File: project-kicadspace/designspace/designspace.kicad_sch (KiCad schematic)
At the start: 0 parts

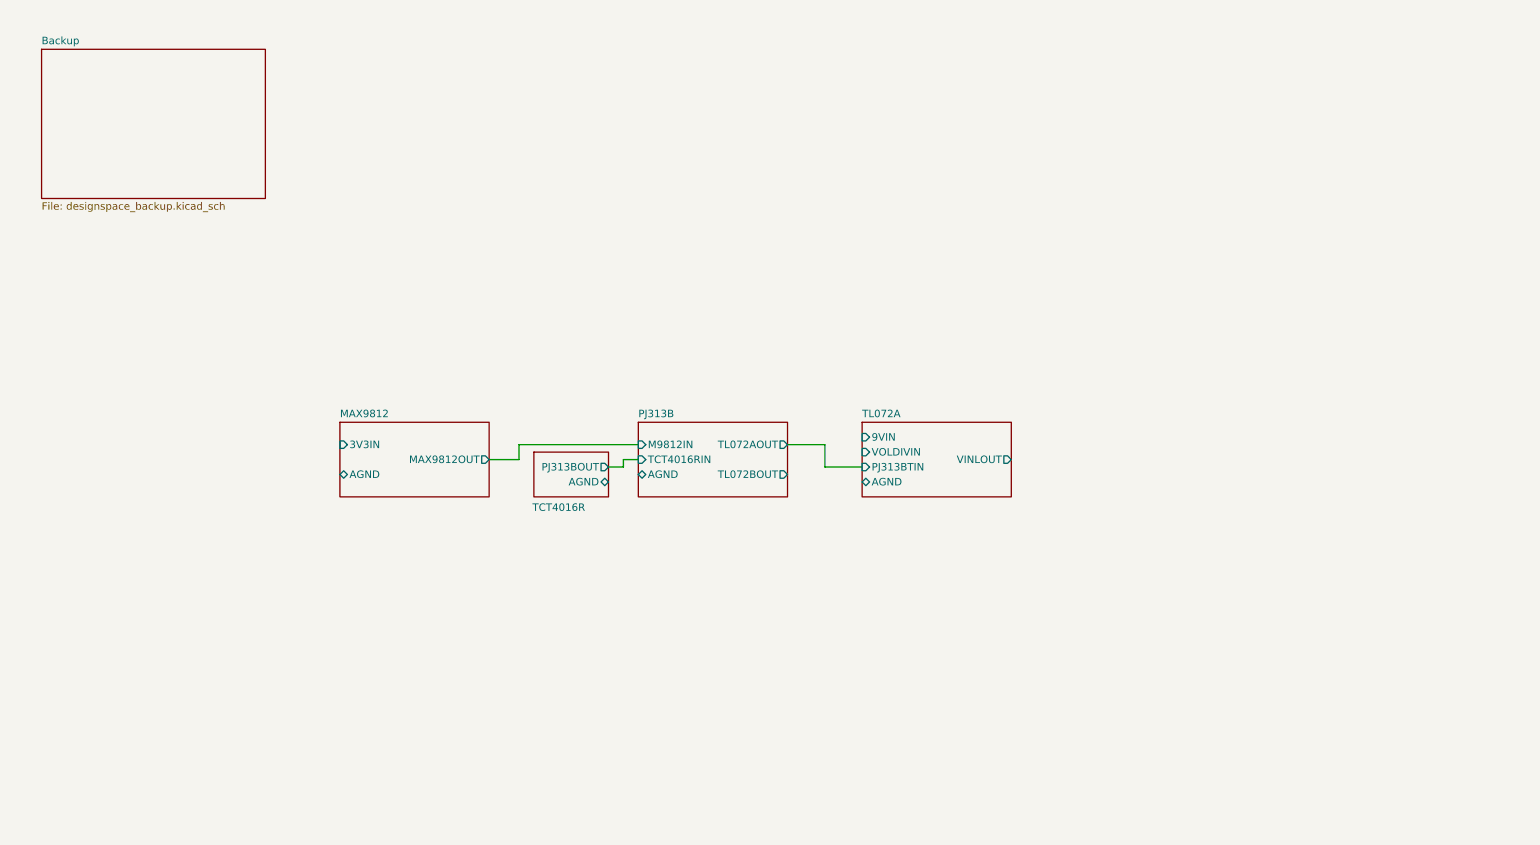
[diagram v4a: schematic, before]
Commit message: feat(sch): remove hierachical structure and add import footprint
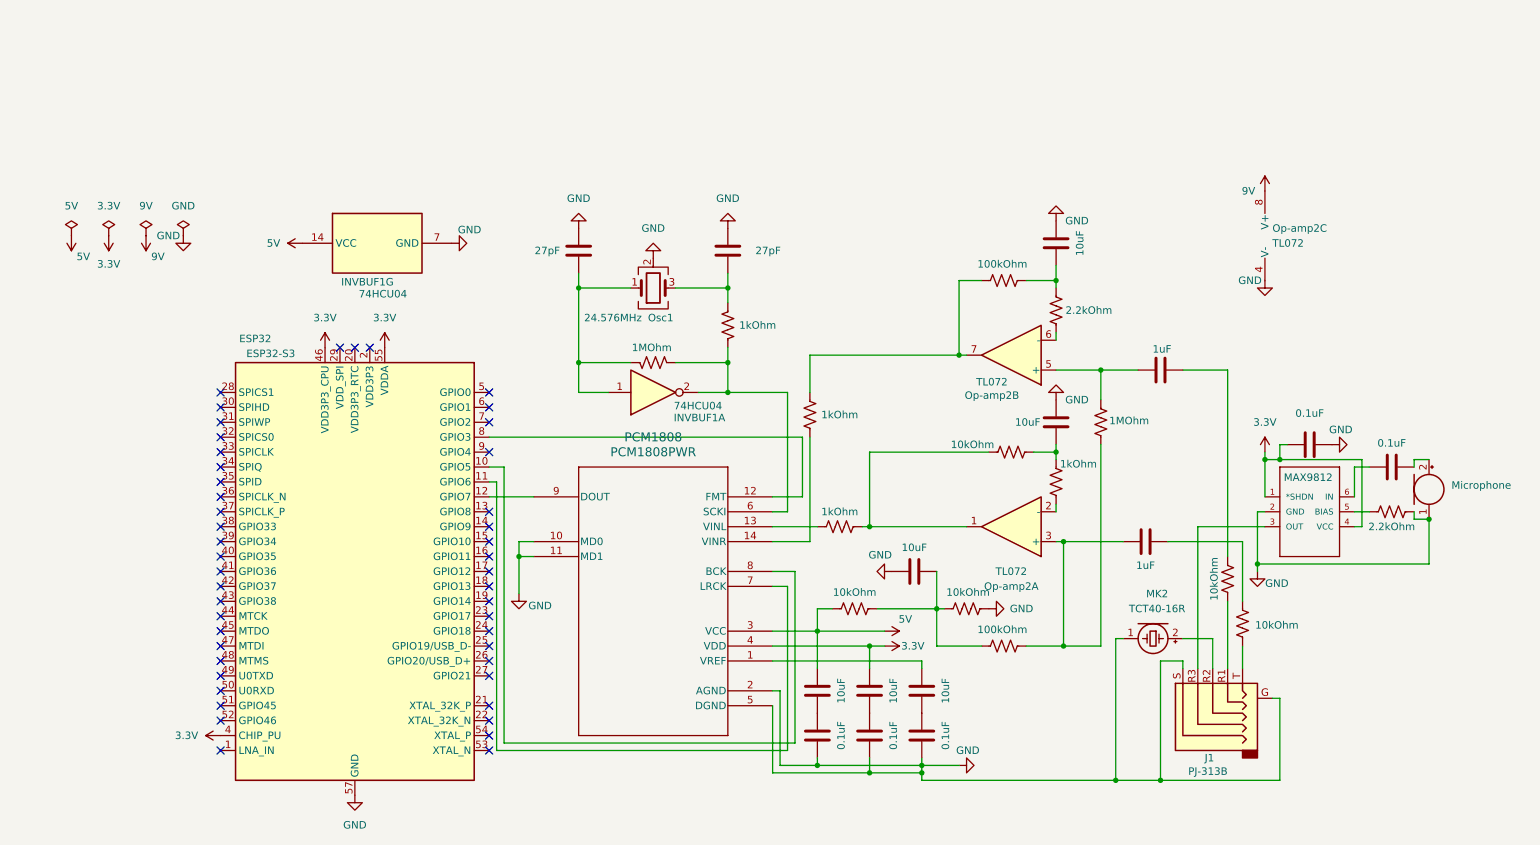
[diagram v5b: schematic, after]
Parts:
- added C1, C2, C5, C7, C9: 0.1uF, Capacitor_SMD:C_0805_2012Metric, symbol Device:C
- added C10, C13, C14, C4, C6, C8: 10uF, Capacitor_SMD:C_0805_2012Metric, symbol Device:C
- added C11, C12: 27pF, Capacitor_SMD:C_0805_2012Metric, symbol Device:C
- added C15, C3: 1uF, Capacitor_SMD:C_0805_2012Metric, symbol Device:C
- added ESP32: ESP32-S3, RF_Module:ESP32-S3-WROOM-1, symbol MCU_Espressif:ESP32-S3
- added INVBUF1: 74HCU04, Package_SO:SO-14_5.3x10.2mm_P1.27mm, symbol 74xx:74HC04
- added J1: PJ-313B, Connector_Audio:Jack_3.5mm_PJ311_Horizontal, symbol Connector_Audio:AudioJack5_Ground
- added MK1: Microphone, Sensor_Audio:POM-2244P-C3310-2-R, symbol Device:Microphone
- added MK2: TCT40-16R, tct4016r:TCT40-16R, symbol Device:Microphone_Ultrasound
- added Op-amp2: TL072, tl072:TL072IDT, symbol Amplifier_Operational:TL072
- added Osc1: 24.576MHz, Crystal:Crystal_SMD_7050-4Pin_7.0x5.0mm, symbol Device:Crystal_GND24
- added PCM1808: PCM1808PWR, pw14:PW14, symbol PCM1808:PCM1808PWR
- added R1, R14: 2.2kOhm, Resistor_SMD:R_0805_2012Metric, symbol Device:R_US
- added R10, R11, R2, R3, R4: 10kOhm, Resistor_SMD:R_0805_2012Metric, symbol Device:R_US
- added R12, R8: 1MOhm, Resistor_SMD:R_0805_2012Metric, symbol Device:R_US
- added R13, R7: 100kOhm, Resistor_SMD:R_0805_2012Metric, symbol Device:R_US
- added R15, R5, R6, R9: 1kOhm, Resistor_SMD:R_0805_2012Metric, symbol Device:R_US
- added U3: MAX9812, tl072:TL072IDT, symbol MAX9812:MAX9812
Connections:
- new net: J1.R3, U3.3 (OUT)
- new net: R1.1, U3.5 (BIAS)
- new net: C1.1, U3.6 (IN)
- new net: C4.2, C5.2
- new net: C15.1, Op-amp2.5 (+), R12.1
- new net: C15.2, R11.1
- new net: C13.2, R2.2, R3.1, R7.1
- new net: ESP32.10 (GPIO5), PCM1808.8 (BCK)
- new net: ESP32.11 (GPIO6), PCM1808.7 (LRCK)
- new net: ESP32.12 (GPIO7), PCM1808.9 (DOUT)
- new net: ESP32.2 (VDD3P3), ESP32.3 (VDD3P3)
- new net: ESP32.8 (GPIO3), PCM1808.12 (FMT)
- new net: C14.2, R13.2, R14.2
- new net: Op-amp2.6 (-), R14.1
- new net: Op-amp2.7, R13.1, R15.2
- new net: C3.1, Op-amp2.3 (+), R12.2, R7.2
- new net: J1.R2, MK2.2 (+)
- new net: C3.2, R10.1
- new net: J1.T, R10.2
- new net: Op-amp2.2 (-), R5.1
- new net: C10.2, R4.2, R5.2
- new net: Op-amp2.1, R4.1, R6.1
- new net: C6.1, PCM1808.1 (VREF)
- new net: PCM1808.13 (VINL), R6.2
- new net: PCM1808.14 (VINR), R15.1
- new net: INVBUF1.2, PCM1808.6 (SCKI), R8.2, R9.2
- new net: C6.2, C7.2
- new net: C8.2, C9.2
- new net: C11.1, INVBUF1.1, Osc1.1, R8.1
- new net: C12.1, Osc1.3, R9.1
- new net: J1.R1, R11.2
- new net: C1.2, MK1.2 (+)
- new net 3.3V: C2.1, C8.1, ESP32.4 (CHIP_PU), ESP32.46 (VDD3P3_CPU), ESP32.55 (VDDA), ESP32.56 (VDDA), PCM1808.4 (VDD), U3.1 (*SHDN), U3.4 (VCC)
- new net 5V: C4.1, INVBUF1.14 (VCC), PCM1808.3 (VCC), R2.1
- new net 9V: Op-amp2.8 (V+)
- new net GND: C10.1, C11.2, C12.2, C13.1, C14.1, C2.2, C5.1, C7.1, C9.1, ESP32.57 (GND), INVBUF1.7 (GND), J1.G, J1.S, MK1.1 (-), MK2.1 (-), Op-amp2.4 (V-), Osc1.2 (G), Osc1.4 (G), PCM1808.10 (MD0), PCM1808.11 (MD1), PCM1808.2 (AGND), PCM1808.5 (DGND), R1.2, R3.2, U3.2 (GND)
- no-connect marks 0 -> 47
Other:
- removed sheet Backup
- removed sheet MAX9812
- removed sheet PJ313B
- removed sheet TCT4016R
- removed sheet TL072A

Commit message: feat(pcb): resolve footprint errors and implement routing between pcm1808, max9812, tct4016r, pj342s
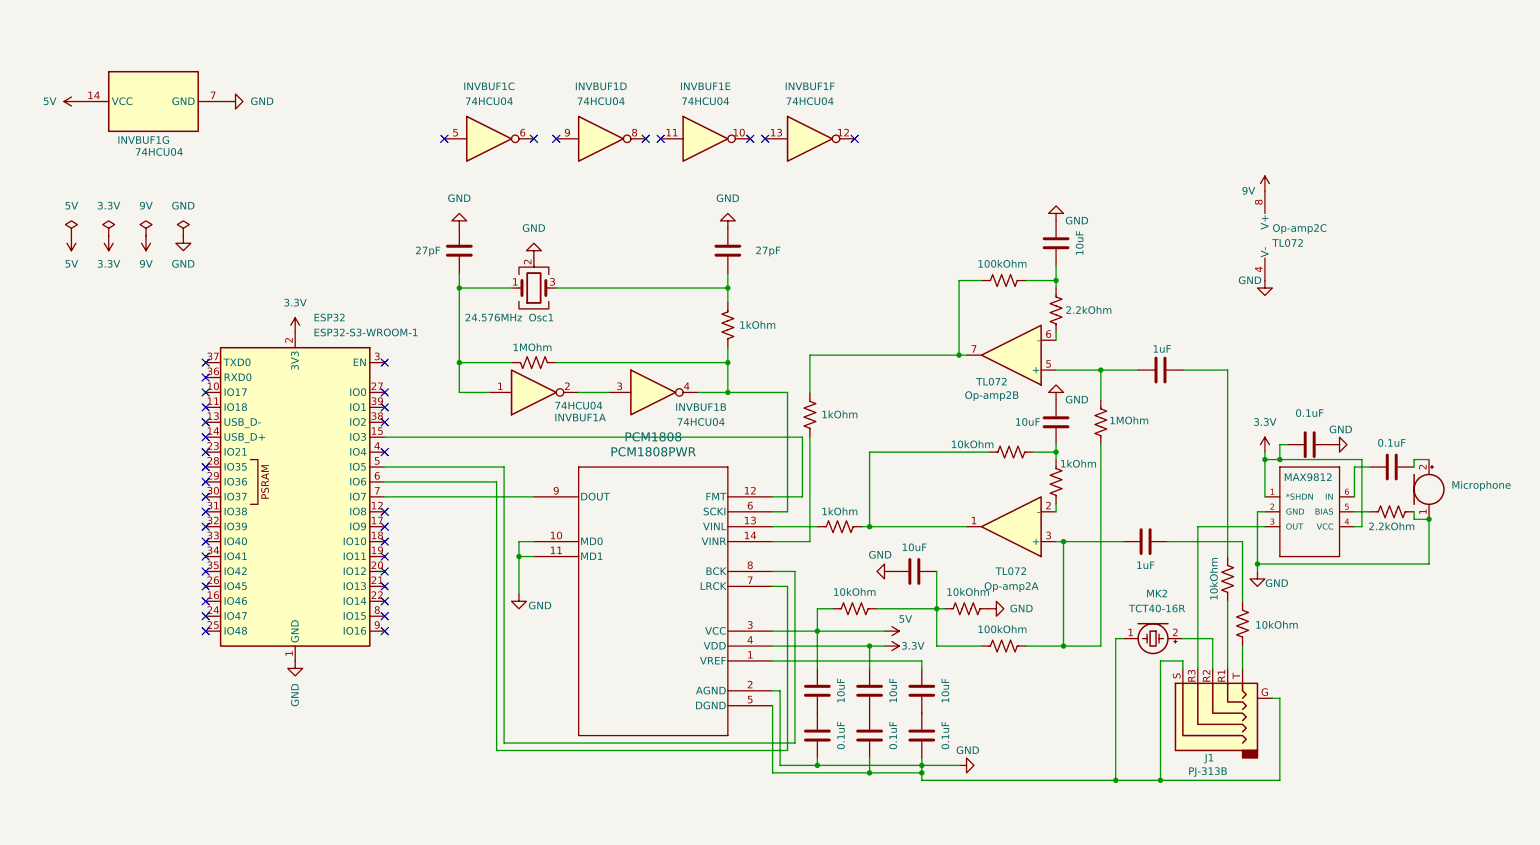
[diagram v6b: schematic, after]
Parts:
- removed ESP32: ESP32-S3, RF_Module:ESP32-S3-WROOM-1, symbol MCU_Espressif:ESP32-S3
- added ESP32: ESP32-S3-WROOM-1, RF_Module:ESP32-S3-WROOM-1, symbol RF_Module:ESP32-S3-WROOM-1
- added unit 3 of INVBUF1
- added unit 6 of INVBUF1
- added unit 5 of INVBUF1
- added unit 2 of INVBUF1
- added unit 4 of INVBUF1
- J1: footprint Connector_Audio:Jack_3.5mm_PJ311_Horizontal -> pj342s:pj342s audio jack
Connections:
- net 3.3V: now also ESP32.2 (3V3)
- net GND: now also ESP32.1 (GND), ESP32.40 (GND), ESP32.41 (GND)
- net at PCM1808.8 (BCK): now also ESP32.5 (IO5)
- net at PCM1808.7 (LRCK): now also ESP32.6 (IO6)
- net at PCM1808.9 (DOUT): now also ESP32.7 (IO7)
- net at PCM1808.12 (FMT): now also ESP32.15 (IO3)
- net at PCM1808.6 (SCKI), R8.2, R9.2: now also INVBUF1.4; no longer INVBUF1.2
- new net: INVBUF1.2, INVBUF1.3
- no-connect marks 47 -> 41
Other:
- moved on the sheet: INVBUF1A, INVBUF1G, Osc1

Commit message: feat(pcb): add kit footprint for esp32 & inital placing
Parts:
- removed ESP32: ESP32-S3-WROOM-1, RF_Module:ESP32-S3-WROOM-1, symbol RF_Module:ESP32-S3-WROOM-1
- added ESP32: ESP32-S3-DEVKITC-1-N8R8, esp32-s3-kit:ESP32-S3-DEVKITC-1-N8R8, symbol ESP32-S3-DEVKITC-1-N8R8:ESP32-S3-DEVKITC-1-N8R8
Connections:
- net 3.3V: now also ESP32.3V3, ESP32.3V3.
- net GND: now also C6.2, ESP32.GND, ESP32.GND1, ESP32.GND2, ESP32.GND3; no longer C7.1, PCM1808.10 (MD0), PCM1808.11 (MD1)
- net at C13.2, R2.2, R3.1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: now also R12.2
- net at C3.1, Op-amp2.3 (+), R7.2: no longer R12.2
- net at PCM1808.1 (VREF): now also C7.2; no longer C6.1
- net at PCM1808.12 (FMT): now also ESP32.GPIO15
- net at PCM1808.7 (LRCK): now also ESP32.GPIO6
- net at PCM1808.8 (BCK): now also ESP32.GPIO5
- net at PCM1808.9 (DOUT): now also ESP32.GPIO7
- new net: ESP32.GPIO16, PCM1808.10 (MD0)
- new net: ESP32.GPIO17, PCM1808.11 (MD1)
- new net: C6.1, C7.1
- no-connect marks 41 -> 40

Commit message: feat(pcb): increase track size for power line & redirect 5V power line to 74HCU04 & PCM1808
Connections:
- net 3.3V: now also INVBUF1.14 (VCC)
- net 5V: now also ESP32.5V0; no longer INVBUF1.14 (VCC)
- net at R13.2, R14.2: now also Op-amp2.6 (-); no longer C14.2
- net at R14.1: now also C14.2; no longer Op-amp2.6 (-)
- net at R5.1: now also C10.2; no longer Op-amp2.2 (-)
- net at R4.2, R5.2: now also Op-amp2.2 (-); no longer C10.2
- no-connect marks 40 -> 39
